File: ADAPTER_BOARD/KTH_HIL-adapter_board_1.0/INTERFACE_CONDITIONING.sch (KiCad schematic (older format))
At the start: 13 parts

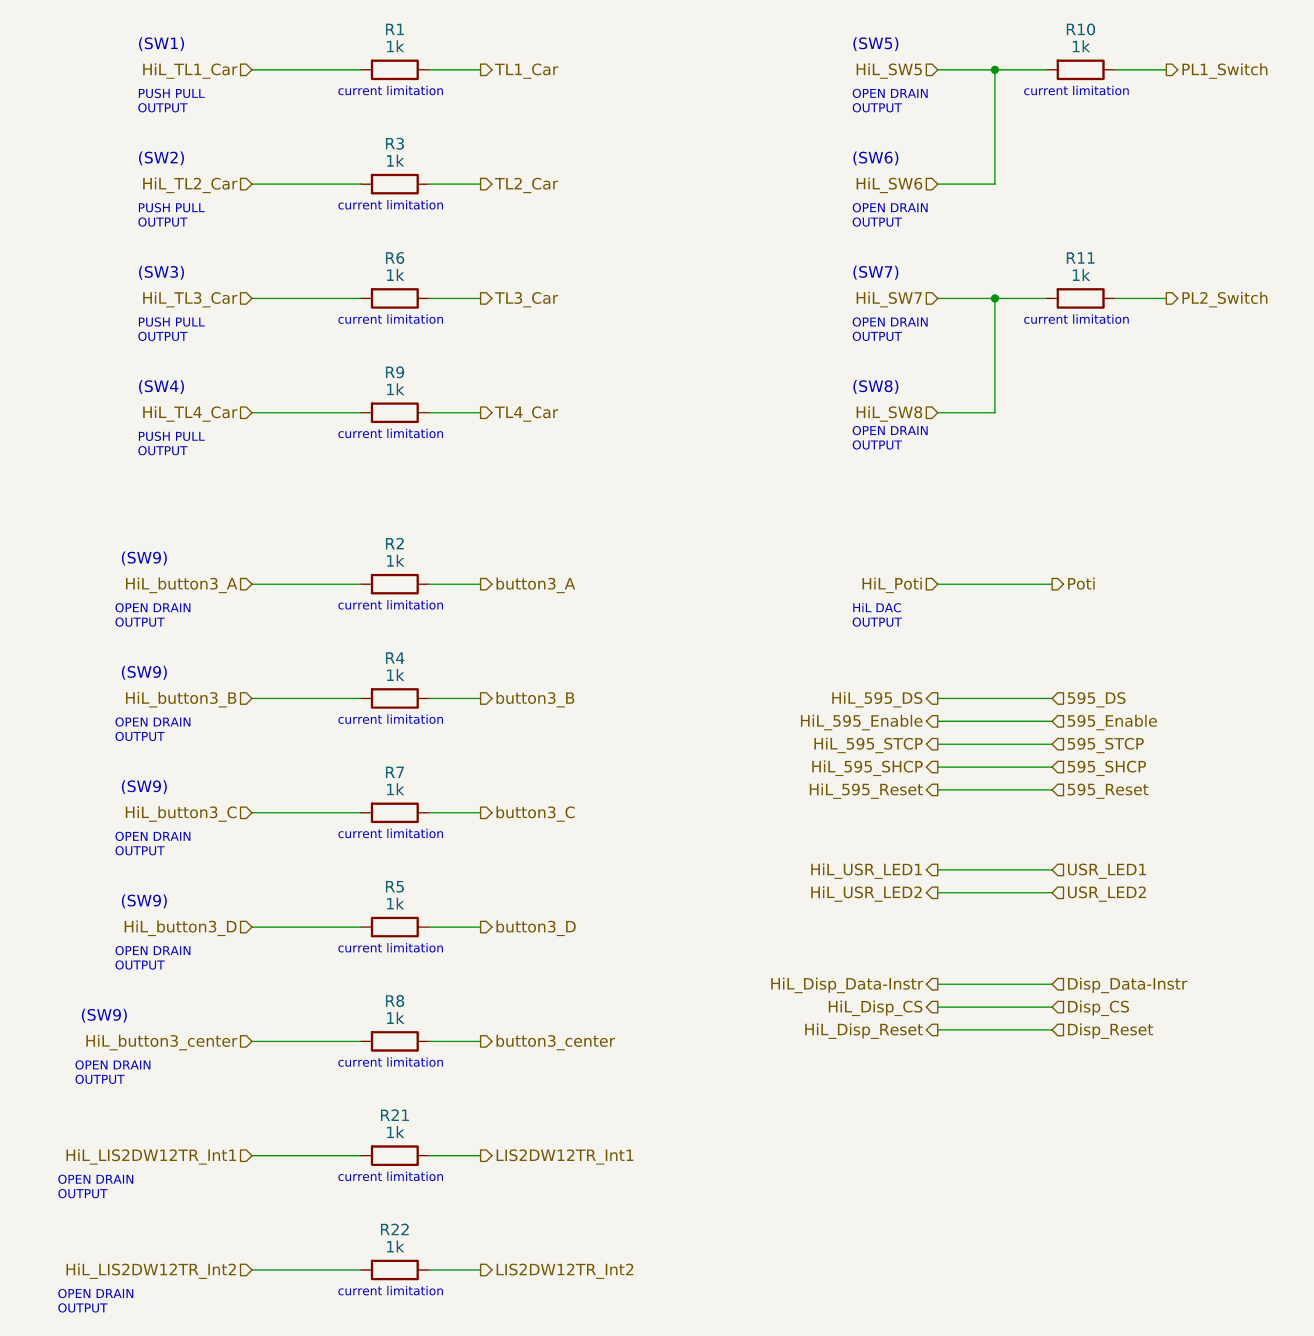
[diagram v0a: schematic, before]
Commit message: Fixed comments regarding schematic
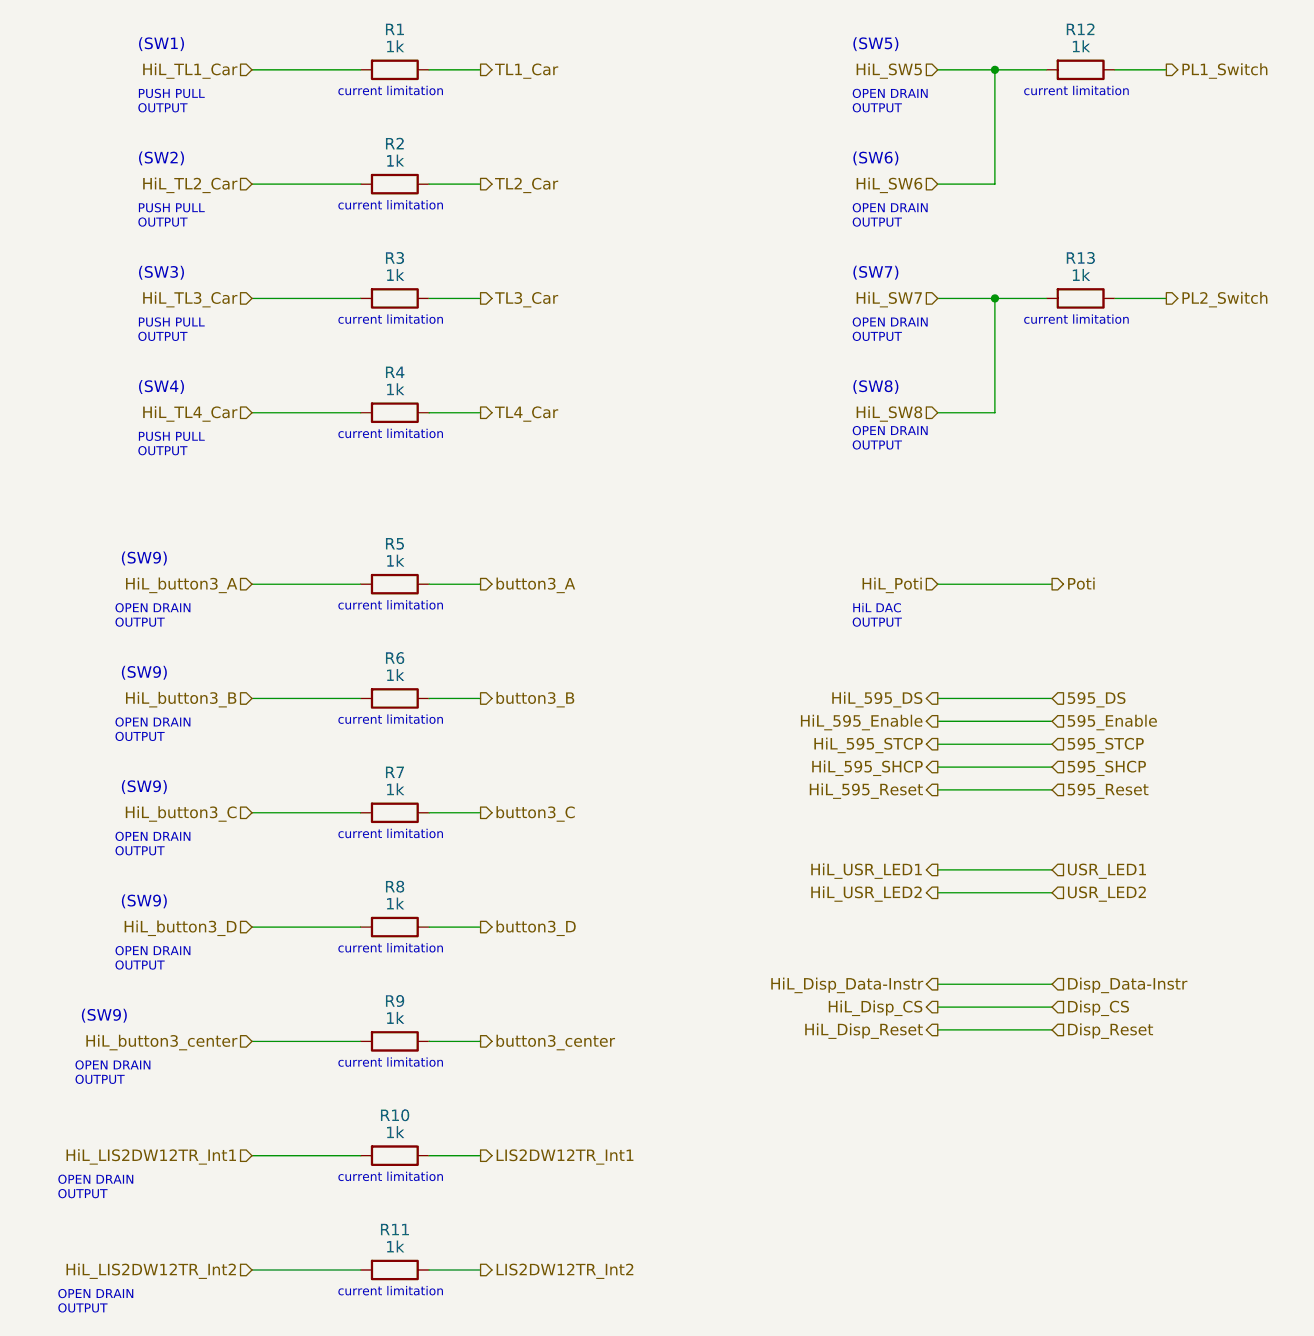
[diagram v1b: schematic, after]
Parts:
- renumbered R21 to R10, R22 to R11, R10 to R12, R11 to R13, R3 to R2, R6 to R3, R9 to R4, R2 to R5, R4 to R6, R5 to R8, R8 to R9
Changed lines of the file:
@@
 EESchema Schematic File Version 4
-LIBS:HIL_ADAPTER_BOARD-cache
 EELAYER 30 0
 EELAYER END
@@
 P 4625 3750
 AR Path="/633B4707/6380467D" Ref="R?"  Part="1"
-AR Path="/63637C97/6380467D" Ref="R2"  Part="1"
+AR Path="/63637C97/6380467D" Ref="R5"  Part="1"
 AR Path="/6350BF25/6380467D" Ref="R?"  Part="1"
 AR Path="/63516F05/6380467D" Ref="R?"  Part="1"
 AR Path="/63516F38/6380467D" Ref="R?"  Part="1"
-F 0 "R2" V 4450 3750 50  0000 C CNN
+F 0 "R5" V 4450 3750 50  0000 C CNN
 F 1 "1k" V 4525 3750 50  0000 C CNN
 F 2 "Resistor_SMD:R_0603_1608Metric" V 4555 3750 50  0001 C CNN
@@
 P 4625 4250
 AR Path="/633B4707/63804684" Ref="R?"  Part="1"
-AR Path="/63637C97/63804684" Ref="R4"  Part="1"
+AR Path="/63637C97/63804684" Ref="R6"  Part="1"
 AR Path="/6350BF25/63804684" Ref="R?"  Part="1"
 AR Path="/63516F05/63804684" Ref="R?"  Part="1"
 AR Path="/63516F38/63804684" Ref="R?"  Part="1"
-F 0 "R4" V 4450 4250 50  0000 C CNN
+F 0 "R6" V 4450 4250 50  0000 C CNN
 F 1 "1k" V 4525 4250 50  0000 C CNN
 F 2 "Resistor_SMD:R_0603_1608Metric" V 4555 4250 50  0001 C CNN
@@
 P 4625 5250
 AR Path="/633B4707/63804693" Ref="R?"  Part="1"
-AR Path="/63637C97/63804693" Ref="R5"  Part="1"
+AR Path="/63637C97/63804693" Ref="R8"  Part="1"
 AR Path="/6350BF25/63804693" Ref="R?"  Part="1"
 AR Path="/63516F05/63804693" Ref="R?"  Part="1"
 AR Path="/63516F38/63804693" Ref="R?"  Part="1"
-F 0 "R5" V 4450 5250 50  0000 C CNN
+F 0 "R8" V 4450 5250 50  0000 C CNN
 F 1 "1k" V 4525 5250 50  0000 C CNN
 F 2 "Resistor_SMD:R_0603_1608Metric" V 4555 5250 50  0001 C CNN
@@
 P 4625 5750
 AR Path="/633B4707/6380469A" Ref="R?"  Part="1"
-AR Path="/63637C97/6380469A" Ref="R8"  Part="1"
+AR Path="/63637C97/6380469A" Ref="R9"  Part="1"
 AR Path="/6350BF25/6380469A" Ref="R?"  Part="1"
 AR Path="/63516F05/6380469A" Ref="R?"  Part="1"
 AR Path="/63516F38/6380469A" Ref="R?"  Part="1"
-F 0 "R8" V 4450 5750 50  0000 C CNN
+F 0 "R9" V 4450 5750 50  0000 C CNN
 F 1 "1k" V 4525 5750 50  0000 C CNN
 F 2 "Resistor_SMD:R_0603_1608Metric" V 4555 5750 50  0001 C CNN
@@
 P 7625 1500
 AR Path="/633B4707/638046A2" Ref="R?"  Part="1"
-AR Path="/63637C97/638046A2" Ref="R10"  Part="1"
+AR Path="/63637C97/638046A2" Ref="R12"  Part="1"
 AR Path="/6350BF25/638046A2" Ref="R?"  Part="1"
 AR Path="/63516F05/638046A2" Ref="R?"  Part="1"
 AR Path="/63516F38/638046A2" Ref="R?"  Part="1"
-F 0 "R10" V 7450 1500 50  0000 C CNN
+F 0 "R12" V 7450 1500 50  0000 C CNN
 F 1 "1k" V 7525 1500 50  0000 C CNN
 F 2 "Resistor_SMD:R_0603_1608Metric" V 7555 1500 50  0001 C CNN
@@
 P 7625 2500
 AR Path="/633B4707/638046A8" Ref="R?"  Part="1"
-AR Path="/63637C97/638046A8" Ref="R11"  Part="1"
+AR Path="/63637C97/638046A8" Ref="R13"  Part="1"
 AR Path="/6350BF25/638046A8" Ref="R?"  Part="1"
 AR Path="/63516F05/638046A8" Ref="R?"  Part="1"
 AR Path="/63516F38/638046A8" Ref="R?"  Part="1"
-F 0 "R11" V 7450 2500 50  0000 C CNN
+F 0 "R13" V 7450 2500 50  0000 C CNN
 F 1 "1k" V 7525 2500 50  0000 C CNN
 F 2 "Resistor_SMD:R_0603_1608Metric" V 7555 2500 50  0001 C CNN
@@
 P 4625 2000
 AR Path="/633B4707/638046C1" Ref="R?"  Part="1"
-AR Path="/63637C97/638046C1" Ref="R3"  Part="1"
+AR Path="/63637C97/638046C1" Ref="R2"  Part="1"
 AR Path="/6350BF25/638046C1" Ref="R?"  Part="1"
 AR Path="/63516F05/638046C1" Ref="R?"  Part="1"
 AR Path="/63516F38/638046C1" Ref="R?"  Part="1"
-F 0 "R3" V 4450 2000 50  0000 C CNN
+F 0 "R2" V 4450 2000 50  0000 C CNN
 F 1 "1k" V 4525 2000 50  0000 C CNN
 F 2 "Resistor_SMD:R_0603_1608Metric" V 4555 2000 50  0001 C CNN
@@
 P 4625 2500
 AR Path="/633B4707/638046CC" Ref="R?"  Part="1"
-AR Path="/63637C97/638046CC" Ref="R6"  Part="1"
+AR Path="/63637C97/638046CC" Ref="R3"  Part="1"
 AR Path="/6350BF25/638046CC" Ref="R?"  Part="1"
 AR Path="/63516F05/638046CC" Ref="R?"  Part="1"
 AR Path="/63516F38/638046CC" Ref="R?"  Part="1"
-F 0 "R6" V 4450 2500 50  0000 C CNN
+F 0 "R3" V 4450 2500 50  0000 C CNN
 F 1 "1k" V 4525 2500 50  0000 C CNN
 F 2 "Resistor_SMD:R_0603_1608Metric" V 4555 2500 50  0001 C CNN
@@
 P 4625 3000
 AR Path="/633B4707/638046D4" Ref="R?"  Part="1"
-AR Path="/63637C97/638046D4" Ref="R9"  Part="1"
+AR Path="/63637C97/638046D4" Ref="R4"  Part="1"
 AR Path="/6350BF25/638046D4" Ref="R?"  Part="1"
 AR Path="/63516F05/638046D4" Ref="R?"  Part="1"
 AR Path="/63516F38/638046D4" Ref="R?"  Part="1"
-F 0 "R9" V 4450 3000 50  0000 C CNN
+F 0 "R4" V 4450 3000 50  0000 C CNN
 F 1 "1k" V 4525 3000 50  0000 C CNN
 F 2 "Resistor_SMD:R_0603_1608Metric" V 4555 3000 50  0001 C CNN
@@
 P 4625 6250
 AR Path="/633B4707/637B3E66" Ref="R?"  Part="1"
-AR Path="/63637C97/637B3E66" Ref="R21"  Part="1"
+AR Path="/63637C97/637B3E66" Ref="R10"  Part="1"
 AR Path="/6350BF25/637B3E66" Ref="R?"  Part="1"
 AR Path="/63516F05/637B3E66" Ref="R?"  Part="1"
 AR Path="/63516F38/637B3E66" Ref="R?"  Part="1"
-F 0 "R21" V 4450 6250 50  0000 C CNN
+F 0 "R10" V 4450 6250 50  0000 C CNN
 F 1 "1k" V 4525 6250 50  0000 C CNN
 F 2 "Resistor_SMD:R_0603_1608Metric" V 4555 6250 50  0001 C CNN
@@
 P 4625 6750
 AR Path="/633B4707/637B555C" Ref="R?"  Part="1"
-AR Path="/63637C97/637B555C" Ref="R22"  Part="1"
+AR Path="/63637C97/637B555C" Ref="R11"  Part="1"
 AR Path="/6350BF25/637B555C" Ref="R?"  Part="1"
 AR Path="/63516F05/637B555C" Ref="R?"  Part="1"
 AR Path="/63516F38/637B555C" Ref="R?"  Part="1"
-F 0 "R22" V 4450 6750 50  0000 C CNN
+F 0 "R11" V 4450 6750 50  0000 C CNN
 F 1 "1k" V 4525 6750 50  0000 C CNN
 F 2 "Resistor_SMD:R_0603_1608Metric" V 4555 6750 50  0001 C CNN
